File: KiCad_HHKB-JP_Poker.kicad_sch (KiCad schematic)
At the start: 21 parts, among them SW1 SW_Push, U1 ATmega32U4-MU, U2 PRTR5V0U2X, Y1 16MHz

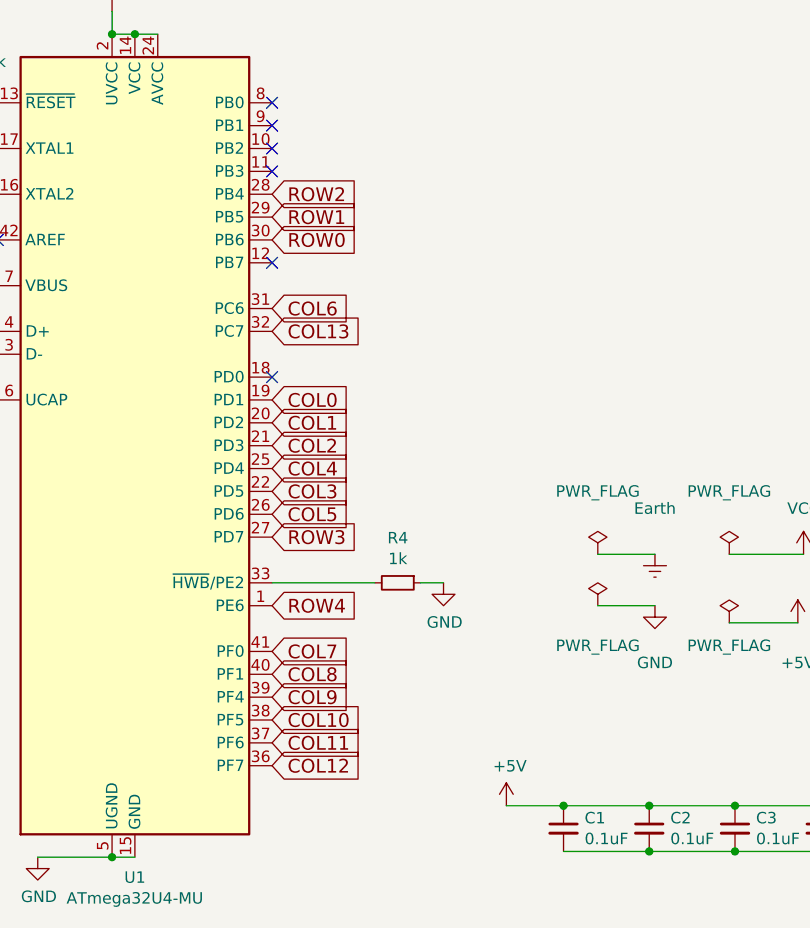
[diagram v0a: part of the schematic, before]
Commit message: 回路図エディターで COL14を追加
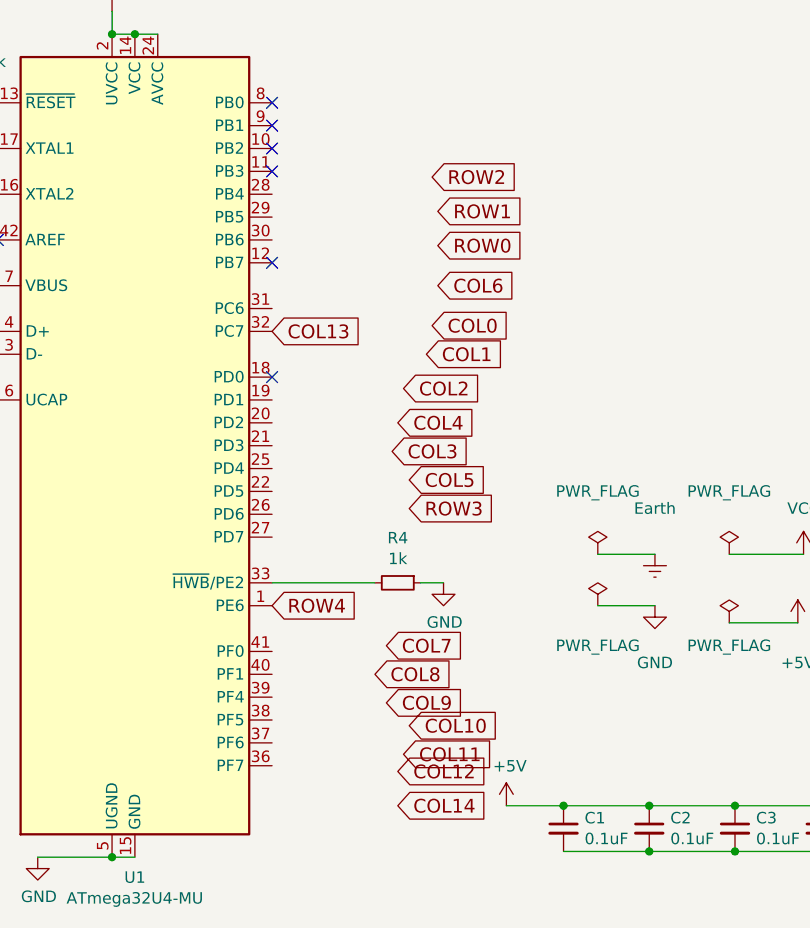
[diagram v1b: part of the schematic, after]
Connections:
- net COL0: no longer U1.19 (PD1)
- net COL1: no longer U1.20 (PD2)
- net COL10: no longer U1.38 (PF5)
- net COL11: no longer U1.37 (PF6)
- net COL12: no longer U1.36 (PF7)
- net COL2: no longer U1.21 (PD3)
- net COL3: no longer U1.22 (PD5)
- net COL4: no longer U1.25 (PD4)
- net COL5: no longer U1.26 (PD6)
- net COL6: no longer U1.31 (PC6)
- net COL7: no longer U1.41 (PF0)
- net COL8: no longer U1.40 (PF1)
- net COL9: no longer U1.39 (PF4)
- net ROW0: no longer U1.30 (PB6)
- net ROW1: no longer U1.29 (PB5)
- net ROW2: no longer U1.28 (PB4)
- net ROW3: no longer U1.27 (PD7)
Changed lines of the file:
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@@
     )
   )
-  (global_label "ROW2" (shape input) (at 76.2 109.22 0) (fields_autoplaced)
+  (global_label "ROW2" (shape input) (at 93.98 107.315 0) (fields_autoplaced)
     (effects (font (size 1.524 1.524)) (justify left))
-    (property "Intersheet References" "${INTERSHEET_REFS}" (id 0) (at 0 0 0)
+    (property "Intersheet References" "${INTERSHEET_REFS}" (id 0) (at 17.78 -1.905 0)
       (effects (font (size 1.27 1.27)) hide)
     )
   )
-  (global_label "COL6" (shape input) (at 76.2 121.92 0) (fields_autoplaced)
+  (global_label "COL6" (shape input) (at 94.615 119.38 0) (fields_autoplaced)
     (effects (font (size 1.524 1.524)) (justify left))
-    (property "Intersheet References" "${INTERSHEET_REFS}" (id 0) (at 0 0 0)
+    (property "Intersheet References" "${INTERSHEET_REFS}" (id 0) (at 18.415 -2.54 0)
       (effects (font (size 1.27 1.27)) hide)
     )
@@
     )
   )
-  (global_label "COL1" (shape input) (at 76.2 134.62 0) (fields_autoplaced)
+  (global_label "COL1" (shape input) (at 93.345 127 0) (fields_autoplaced)
     (effects (font (size 1.524 1.524)) (justify left))
-    (property "Intersheet References" "${INTERSHEET_REFS}" (id 0) (at 84.7946 134.5248 0)
+    (property "Intersheet References" "${INTERSHEET_REFS}" (id 0) (at 101.9396 126.9048 0)
       (effects (font (size 1.524 1.524)) (justify left) hide)
     )
   )
-  (global_label "COL4" (shape input) (at 76.2 139.7 0) (fields_autoplaced)
+  (global_label "COL4" (shape input) (at 90.17 134.62 0) (fields_autoplaced)
     (effects (font (size 1.524 1.524)) (justify left))
-    (property "Intersheet References" "${INTERSHEET_REFS}" (id 0) (at 0 0 0)
+    (property "Intersheet References" "${INTERSHEET_REFS}" (id 0) (at 13.97 -5.08 0)
       (effects (font (size 1.27 1.27)) hide)
     )
   )
-  (global_label "ROW0" (shape input) (at 76.2 114.3 0) (fields_autoplaced)
+  (global_label "ROW0" (shape input) (at 94.615 114.935 0) (fields_autoplaced)
     (effects (font (size 1.524 1.524)) (justify left))
-    (property "Intersheet References" "${INTERSHEET_REFS}" (id 0) (at 0 0 0)
+    (property "Intersheet References" "${INTERSHEET_REFS}" (id 0) (at 18.415 0.635 0)
       (effects (font (size 1.27 1.27)) hide)
     )
@@
     )
   )
-  (global_label "COL3" (shape input) (at 76.2 142.24 0) (fields_autoplaced)
+  (global_label "COL3" (shape input) (at 89.535 137.795 0) (fields_autoplaced)
     (effects (font (size 1.524 1.524)) (justify left))
-    (property "Intersheet References" "${INTERSHEET_REFS}" (id 0) (at 0 0 0)
+    (property "Intersheet References" "${INTERSHEET_REFS}" (id 0) (at 13.335 -4.445 0)
       (effects (font (size 1.27 1.27)) hide)
     )
   )
-  (global_label "ROW3" (shape input) (at 76.2 147.32 0) (fields_autoplaced)
+  (global_label "ROW3" (shape input) (at 91.44 144.145 0) (fields_autoplaced)
     (effects (font (size 1.524 1.524)) (justify left))
-    (property "Intersheet References" "${INTERSHEET_REFS}" (id 0) (at 0 0 0)
+    (property "Intersheet References" "${INTERSHEET_REFS}" (id 0) (at 15.24 -3.175 0)
       (effects (font (size 1.27 1.27)) hide)
     )
   )
-  (global_label "COL8" (shape input) (at 76.2 162.56 0) (fields_autoplaced)
+  (global_label "COL8" (shape input) (at 87.63 162.56 0) (fields_autoplaced)
     (effects (font (size 1.524 1.524)) (justify left))
-    (property "Intersheet References" "${INTERSHEET_REFS}" (id 0) (at 0 0 0)
+    (property "Intersheet References" "${INTERSHEET_REFS}" (id 0) (at 11.43 0 0)
       (effects (font (size 1.27 1.27)) hide)
     )
   )
-  (global_label "COL12" (shape input) (at 76.2 172.72 0) (fields_autoplaced)
+  (global_label "COL12" (shape input) (at 90.17 173.355 0) (fields_autoplaced)
     (effects (font (size 1.524 1.524)) (justify left))
-    (property "Intersheet References" "${INTERSHEET_REFS}" (id 0) (at 0 0 0)
+    (property "Intersheet References" "${INTERSHEET_REFS}" (id 0) (at 13.97 0.635 0)
       (effects (font (size 1.27 1.27)) hide)
     )
   )
-  (global_label "COL5" (shape input) (at 76.2 144.78 0) (fields_autoplaced)
+  (global_label "COL14" (shape input) (at 90.17 177.165 0) (fields_autoplaced)
     (effects (font (size 1.524 1.524)) (justify left))
-    (property "Intersheet References" "${INTERSHEET_REFS}" (id 0) (at 0 0 0)
+    (property "Intersheet References" "${INTERSHEET_REFS}" (id 0) (at 100.216 177.0698 0)
+      (effects (font (size 1.524 1.524)) (justify left) hide)
+    )
+  )
+  (global_label "COL5" (shape input) (at 91.44 140.97 0) (fields_autoplaced)
+    (effects (font (size 1.524 1.524)) (justify left))
+    (property "Intersheet References" "${INTERSHEET_REFS}" (id 0) (at 15.24 -3.81 0)
       (effects (font (size 1.27 1.27)) hide)
     )
   )
-  (global_label "COL7" (shape input) (at 76.2 160.02 0) (fields_autoplaced)
+  (global_label "COL7" (shape input) (at 88.9 159.385 0) (fields_autoplaced)
     (effects (font (size 1.524 1.524)) (justify left))
-    (property "Intersheet References" "${INTERSHEET_REFS}" (id 0) (at 0 0 0)
+    (property "Intersheet References" "${INTERSHEET_REFS}" (id 0) (at 12.7 -0.635 0)
       (effects (font (size 1.27 1.27)) hide)
     )
   )
-  (global_label "COL9" (shape input) (at 76.2 165.1 0) (fields_autoplaced)
+  (global_label "COL9" (shape input) (at 88.9 165.735 0) (fields_autoplaced)
     (effects (font (size 1.524 1.524)) (justify left))
-    (property "Intersheet References" "${INTERSHEET_REFS}" (id 0) (at 0 0 0)
+    (property "Intersheet References" "${INTERSHEET_REFS}" (id 0) (at 12.7 0.635 0)
       (effects (font (size 1.27 1.27)) hide)
     )
@@
     )
   )
-  (global_label "COL2" (shape input) (at 76.2 137.16 0) (fields_autoplaced)
+  (global_label "COL2" (shape input) (at 90.805 130.81 0) (fields_autoplaced)
     (effects (font (size 1.524 1.524)) (justify left))
-    (property "Intersheet References" "${INTERSHEET_REFS}" (id 0) (at 0 0 0)
+    (property "Intersheet References" "${INTERSHEET_REFS}" (id 0) (at 14.605 -6.35 0)
       (effects (font (size 1.27 1.27)) hide)
     )
@@
     )
   )
-  (global_label "COL0" (shape input) (at 76.2 132.08 0) (fields_autoplaced)
+  (global_label "COL0" (shape input) (at 93.98 123.825 0) (fields_autoplaced)
     (effects (font (size 1.524 1.524)) (justify left))
-    (property "Intersheet References" "${INTERSHEET_REFS}" (id 0) (at 84.7946 131.9848 0)
+    (property "Intersheet References" "${INTERSHEET_REFS}" (id 0) (at 102.5746 123.7298 0)
       (effects (font (size 1.524 1.524)) (justify left) hide)
     )
   )
-  (global_label "COL10" (shape input) (at 76.2 167.64 0) (fields_autoplaced)
+  (global_label "COL10" (shape input) (at 91.44 168.275 0) (fields_autoplaced)
     (effects (font (size 1.524 1.524)) (justify left))
-    (property "Intersheet References" "${INTERSHEET_REFS}" (id 0) (at 0 0 0)
+    (property "Intersheet References" "${INTERSHEET_REFS}" (id 0) (at 15.24 0.635 0)
       (effects (font (size 1.27 1.27)) hide)
     )
   )
-  (global_label "COL11" (shape input) (at 76.2 170.18 0) (fields_autoplaced)
+  (global_label "COL11" (shape input) (at 90.805 171.45 0) (fields_autoplaced)
     (effects (font (size 1.524 1.524)) (justify left))
-    (property "Intersheet References" "${INTERSHEET_REFS}" (id 0) (at 0 0 0)
+    (property "Intersheet References" "${INTERSHEET_REFS}" (id 0) (at 14.605 1.27 0)
       (effects (font (size 1.27 1.27)) hide)
     )
   )
-  (global_label "ROW1" (shape input) (at 76.2 111.76 0) (fields_autoplaced)
+  (global_label "ROW1" (shape input) (at 94.615 111.125 0) (fields_autoplaced)
     (effects (font (size 1.524 1.524)) (justify left))
-    (property "Intersheet References" "${INTERSHEET_REFS}" (id 0) (at 0 0 0)
+    (property "Intersheet References" "${INTERSHEET_REFS}" (id 0) (at 18.415 -0.635 0)
       (effects (font (size 1.27 1.27)) hide)
     )

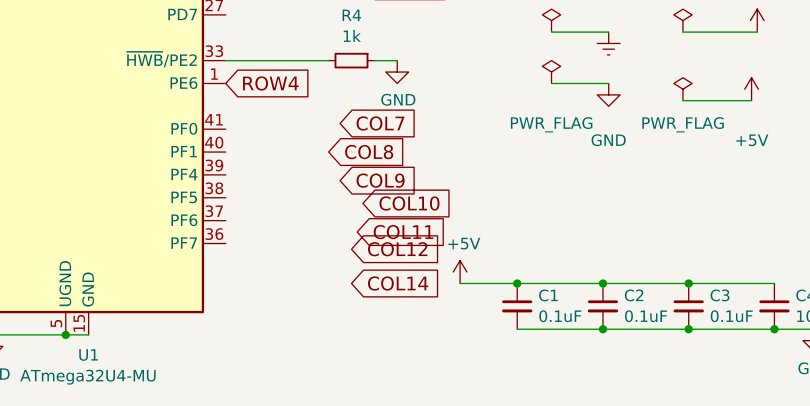
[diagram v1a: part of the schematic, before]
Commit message: 回路図エディターで COL14削除、結局 JP60から、 ]と backspace の位置だけ変更した
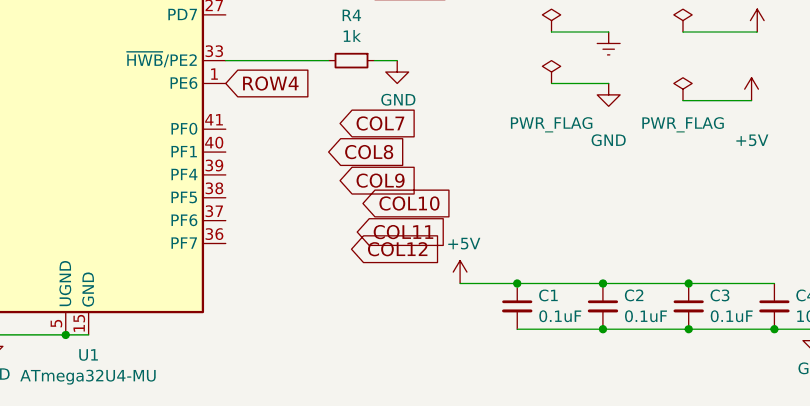
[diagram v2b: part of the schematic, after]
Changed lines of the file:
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@@
-    )
-  )
-  (global_label "COL14" (shape input) (at 90.17 177.165 0) (fields_autoplaced)
-    (effects (font (size 1.524 1.524)) (justify left))
-    (property "Intersheet References" "${INTERSHEET_REFS}" (id 0) (at 100.216 177.0698 0)
-      (effects (font (size 1.524 1.524)) (justify left) hide)
     )
   )
@@
       (reference "K_B1") (unit 1) (value "MX-NoLED") (footprint "MX_Only:MXOnly-1U-Hotswap")
     )
+    (path "/00000000-0000-0000-0000-00005a286589/00000000-0000-0000-0000-00005fb7e4d3"
+      (reference "K_BKSL1") (unit 1) (value "MX-NoLED") (footprint "MX_Only:MXOnly-1U-Hotswap")
+    )
     (path "/00000000-0000-0000-0000-00005a286589/00000000-0000-0000-0000-00005fad7e11"
       (reference "K_BKSPC1") (unit 1) (value "MX-NoLED") (footprint "MX_Only:MXOnly-1U-Hotswap")
@@
       (reference "K_P1") (unit 1) (value "MX-NoLED") (footprint "MX_Only:MXOnly-1U-Hotswap")
     )
-    (path "/00000000-0000-0000-0000-00005a286589/00000000-0000-0000-0000-00005d45f606"
-      (reference "K_PIPE1") (unit 1) (value "MX-NoLED") (footprint "MX_Only:MXOnly-1U-Hotswap")
-    )
     (path "/00000000-0000-0000-0000-00005a286589/00000000-0000-0000-0000-00005d47fe23"
       (reference "K_Q1") (unit 1) (value "MX-NoLED") (footprint "MX_Only:MXOnly-1U-Hotswap")
@@
       (reference "K_U1") (unit 1) (value "MX-NoLED") (footprint "MX_Only:MXOnly-1U-Hotswap")
     )
-    (path "/00000000-0000-0000-0000-00005a286589/00000000-0000-0000-0000-00005fb7e4d3"
-      (reference "K_UNSC1") (unit 1) (value "MX-NoLED") (footprint "MX_Only:MXOnly-1U-Hotswap")
-    )
     (path "/00000000-0000-0000-0000-00005a286589/2509ecc1-7b87-4597-b2e5-0d72327a0dc3"
       (reference "K_UP1") (unit 1) (value "MX-NoLED") (footprint "MX_Only:MXOnly-1U-Hotswap")
@@
       (reference "K_Y1") (unit 1) (value "MX-NoLED") (footprint "MX_Only:MXOnly-1U-Hotswap")
     )
+    (path "/00000000-0000-0000-0000-00005a286589/00000000-0000-0000-0000-00005d45f606"
+      (reference "K_YEN1") (unit 1) (value "MX-NoLED") (footprint "MX_Only:MXOnly-1U-Hotswap")
+    )
     (path "/00000000-0000-0000-0000-00005a286589/00000000-0000-0000-0000-00005d497b94"
